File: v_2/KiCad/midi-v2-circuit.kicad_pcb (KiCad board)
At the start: 2 copper layers, 40 parts, among them CON1 IDC-14, CON2 AVR-ISP-10, CON3 IDC-14, J1 Screw_Terminal_01x12, J2 Conn_01x04, J3 DIN-8, J4 Conn_01x17, J6 USB_B, J7 to_midi_adapter_USB, J8 to_midi_adapter_MIDI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

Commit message: pcb first version complete - ready for hardware check and further optimalisation do 10x10cm
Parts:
- added REF**: MountingHole_4mm, Mounting_Holes:MountingHole_4mm, F.Cu at (255.9, 82.7)
- added REF**: MountingHole_2.5mm, Mounting_Holes:MountingHole_2.5mm, F.Cu at (269.4, 115.0)
- added REF**: MountingHole_4mm, Mounting_Holes:MountingHole_4mm, F.Cu at (255.9, 175.4)
- added REF**: MountingHole_4mm, Mounting_Holes:MountingHole_4mm, F.Cu at (347.3, 82.7)
- added REF**: MountingHole_4mm, Mounting_Holes:MountingHole_4mm, F.Cu at (347.3, 175.4)
- added REF**: MountingHole_2.5mm, Mounting_Holes:MountingHole_2.5mm, F.Cu at (269.4, 157.2)
- added REF**: MountingHole_2.5mm, Mounting_Holes:MountingHole_2.5mm, F.Cu at (284.7, 157.2)
- added REF**: MountingHole_2.5mm, Mounting_Holes:MountingHole_2.5mm, F.Cu at (284.7, 115.0)
- C1, C2, C5, C6, R1, R2, R3, R5, R8, R9: moved to B.Cu
- moved C10 231.3 mm to (332.7, 38.9)
- moved C11 231.3 mm to (332.7, 33.1)
- moved CON1 231.3 mm to (343.3, 54.8)
- moved J1 231.3 mm to (313.8, 68.5)
- moved C8 231.3 mm to (337.1, 33.1)
- moved C9 231.3 mm to (337.1, 38.9)
- moved REF** 231.3 mm to (306.1, 71.6)
- moved REF** 231.3 mm to (346.7, 30.9)
- moved REF** 231.3 mm to (306.1, 30.9)
- moved REF** 231.3 mm to (346.7, 71.6)
- moved RV1 231.3 mm to (326.4, 51.2)
- moved J7 91.5 mm to (273.4, 170.6), turned to 270 degrees
- moved CON3 67.4 mm to (343.6, 164.7), turned to 180 degrees
- moved R1 47.6 mm to (340.2, 115.4), turned to 180 degrees
- moved D1 35.6 mm to (267.8, 87.6)
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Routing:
- net GND: track 410.2 -> 603.6 mm, vias 0 -> 1
- net Net-(J6-Pad3): track 13.1 -> 114.2 mm
- net Net-(J6-Pad2): track 11.2 -> 111.8 mm
- net midi-raw-signal-power: track 29.6 -> 75.9 mm
- net SCL: track 21.2 -> 53.3 mm, vias 0 -> 1
- net joystick-pot-1: track 95.8 -> 68.0 mm
- net +5V: track 424.2 -> 450.2 mm, vias 0 -> 3
- net joystick-pot-2: track 86.2 -> 62.3 mm
- net button-4: track 79.9 -> 103.8 mm
- net MISO: track 122.9 -> 146.6 mm
- net Net-(D1-Pad2): track 10.8 -> 33.6 mm
- net RST: track 83.7 -> 63.4 mm
- net button-3: track 74.2 -> 94.3 mm
- net VCC: track 47.2 -> 27.7 mm
- net knob-pot-4: track 79.0 -> 61.0 mm
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
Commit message: adc first success
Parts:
- removed the REF** at (255.9, 82.7)
- removed the REF** at (306.1, 71.6)
- removed the REF** at (255.9, 175.4)
- removed the REF** at (347.3, 82.7)
- removed the REF** at (347.3, 175.4)
- removed the REF** at (346.7, 30.9)
- removed the REF** at (306.1, 30.9)
- removed the REF** at (346.7, 71.6)
- added R10: 330, Resistors_SMD:R_0805_HandSoldering, B.Cu at (97.0, 95.2)
- added R11: 330, Resistors_SMD:R_0805_HandSoldering, B.Cu at (97.0, 93.0)
- added R12: 330, Resistors_SMD:R_0805_HandSoldering, B.Cu at (97.0, 90.7)
- added R13: 330, Resistors_SMD:R_0805_HandSoldering, B.Cu at (97.0, 88.4)
- added R6: 330, Resistors_SMD:R_0805_HandSoldering, B.Cu at (97.0, 99.8)
- added R7: 330, Resistors_SMD:R_0805_HandSoldering, B.Cu at (97.0, 97.5)
- added REF**: MountingHole_4mm, Mounting_Holes:MountingHole_4mm, F.Cu at (193.2, 107.6)
- added REF**: MountingHole_2.2mm_M2, Mounting_Holes:MountingHole_2.2mm_M2, F.Cu at (106.6, 107.2)
- added REF**: MountingHole_2.2mm_M2, Mounting_Holes:MountingHole_2.2mm_M2, F.Cu at (87.5, 81.8)
- added REF**: MountingHole_2.2mm_M2, Mounting_Holes:MountingHole_2.2mm_M2, F.Cu at (106.6, 81.8)
- added REF**: MountingHole_2.2mm_M2, Mounting_Holes:MountingHole_2.2mm_M2, F.Cu at (87.5, 107.2)
- added REF**: MountingHole_4mm, Mounting_Holes:MountingHole_4mm, F.Cu at (132.5, 107.6)
- added REF**: MountingHole_4mm, Mounting_Holes:MountingHole_4mm, F.Cu at (81.7, 58.0)
- added REF**: MountingHole_4mm, Mounting_Holes:MountingHole_4mm, F.Cu at (193.2, 58.0)
- C3, C4, C7, R4: moved to B.Cu
- L1: footprint Inductors_SMD:L_1812_HandSoldering -> Inductors_SMD:L_0805_HandSoldering; moved to B.Cu
- moved CON1 261.2 mm to (84.1, 87.4), turned to 180 degrees
- moved C8 251.4 mm to (97.0, 107.8), turned to 90 degrees
- moved C9 244.0 mm to (103.0, 107.8), turned to 90 degrees
- moved C11 234.7 mm to (108.6, 102.5), turned to 0 degrees
- moved RV1 233.4 mm to (97.0, 94.5), turned to 180 degrees
- moved C10 232.2 mm to (108.7, 99.8), turned to 0 degrees
- moved R2 225.5 mm to (90.1, 66.7), turned to 180 degrees
- moved J2 222.0 mm to (83.8, 66.8), turned to 0 degrees
- moved R3 220.7 mm to (90.1, 70.9), turned to 180 degrees
- moved J1 200.8 mm to (113.4, 81.0), turned to 270 degrees
- moved R1 175.8 mm to (172.0, 64.4), turned to 270 degrees
- moved C4 173.7 mm to (157.7, 78.5), turned to 270 degrees
- moved SW2 172.9 mm to (176.3, 58.4), turned to 0 degrees
- moved C6 172.6 mm to (177.0, 78.6), turned to 90 degrees
- moved Y1 172.6 mm to (150.5, 73.5)
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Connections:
- J1 pad 10: button-2 -> button-4
- J1 pad 11: button-3 -> button-1
- J1 pad 12: button-4 -> button-2
- J1 pad 3: slide-pot-1 -> Net-(J1-Pad3)
- J1 pad 4: slide-pot-2 -> Net-(J1-Pad4)
- J1 pad 5: knob-pot-1 -> Net-(J1-Pad5)
- J1 pad 6: knob-pot-2 -> Net-(J1-Pad6)
- J1 pad 7: knob-pot-3 -> Net-(J1-Pad7)
- J1 pad 8: knob-pot-4 -> Net-(J1-Pad8)
- J1 pad 9: button-1 -> button-3
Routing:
- net GND: track 603.6 -> 123.3 mm, vias 1 -> 3
- net Net-(J6-Pad2): track 111.8 -> 24.5 mm
- net Net-(J6-Pad3): track 114.2 -> 30.0 mm
- net SDA: track 35.5 -> 117.1 mm
- net MOSI: track 169.6 -> 88.2 mm, vias 0 -> 1
- net MISO: track 146.6 -> 73.6 mm, vias 0 -> 1
- net +5V: track 450.2 -> 388.7 mm
- net SCL: track 53.3 -> 112.0 mm
- net button-2: track 112.4 -> 57.2 mm
- net SCK: track 140.3 -> 85.9 mm, vias 0 -> 1
- net button-1: track 99.4 -> 53.3 mm
- net slide-pot-1: track 76.4 -> 34.0 mm
- net slide-pot-2: track 74.5 -> 34.6 mm
- net midi-raw-signal-power: track 75.9 -> 37.3 mm
- net knob-pot-1: track 69.9 -> 34.0 mm
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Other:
- board outline added: 120.4 x 58.4 mm
- net class Default: via_dia 0.6 -> 1.2
- board text added: "MIDI v2"
- board text added: "by MM"

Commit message: improvements before first pcb order
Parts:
- removed the REF** at (138.3, 81.0)
- removed the REF** at (180.8, 98.5)
- added R14: 10k, Resistors_SMD:R_0805_HandSoldering, B.Cu at (143.3, 105.9)
- added R15: 10k, Resistors_SMD:R_0805_HandSoldering, B.Cu at (155.8, 70.9)
- added R16: 10k, Resistors_SMD:R_0805_HandSoldering, B.Cu at (163.0, 70.9)
- added R17: 10k, Resistors_SMD:R_0805_HandSoldering, B.Cu at (159.6, 70.9)
- added REF**: MountingHole_2.5mm, Mounting_Holes:MountingHole_2.5mm, F.Cu at (178.9, 83.2)
- added REF**: MountingHole_2.5mm, Mounting_Holes:MountingHole_2.5mm, F.Cu at (178.9, 95.3)
- moved REF** 45.0 mm to (135.9, 83.2)
- moved REF** 3.95 mm to (136.0, 95.3)
- moved J4 2.00 mm to (174.4, 105.9)
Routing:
- net GND: track 123.3 -> 164.4 mm
- net octave-1: track 59.6 -> 78.2 mm
- net SCK: track 85.9 -> 102.2 mm
- net MISO: track 73.6 -> 88.3 mm
- net MOSI: track 88.2 -> 100.8 mm
- net note-13: track 28.4 -> 31.7 mm
- net note-7: track 32.8 -> 36.1 mm
- net knob-pot-1: track 34.0 -> 36.9 mm
- net knob-pot-3: track 35.3 -> 37.8 mm
- net knob-pot-2: track 33.3 -> 35.6 mm
- net note-6: track 36.9 -> 38.9 mm
- net note-9: track 27.8 -> 29.8 mm
- net note-8: track 31.9 -> 33.9 mm
- net note-5: track 34.8 -> 36.8 mm
- net note-3: track 36.8 -> 38.8 mm
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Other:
- board text added: "MM 2018"
- board text removed: "by MM"

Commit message: tweaks before first order part 2
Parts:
- moved REF** 5.02 mm to (136.0, 78.2)
- moved REF** 4.95 mm to (179.0, 78.3)
- moved C6 3.18 mm to (173.9, 78.5)
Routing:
- net button-1: track 53.5 -> 62.0 mm
- net slide-pot-1: track 34.0 -> 38.5 mm
- net +5V: track 388.3 -> 384.5 mm
- net slide-pot-2: track 33.9 -> 37.5 mm
- net GND: track 164.4 -> 161.2 mm
- net midi-data-pin: track 51.6 -> 49.0 mm

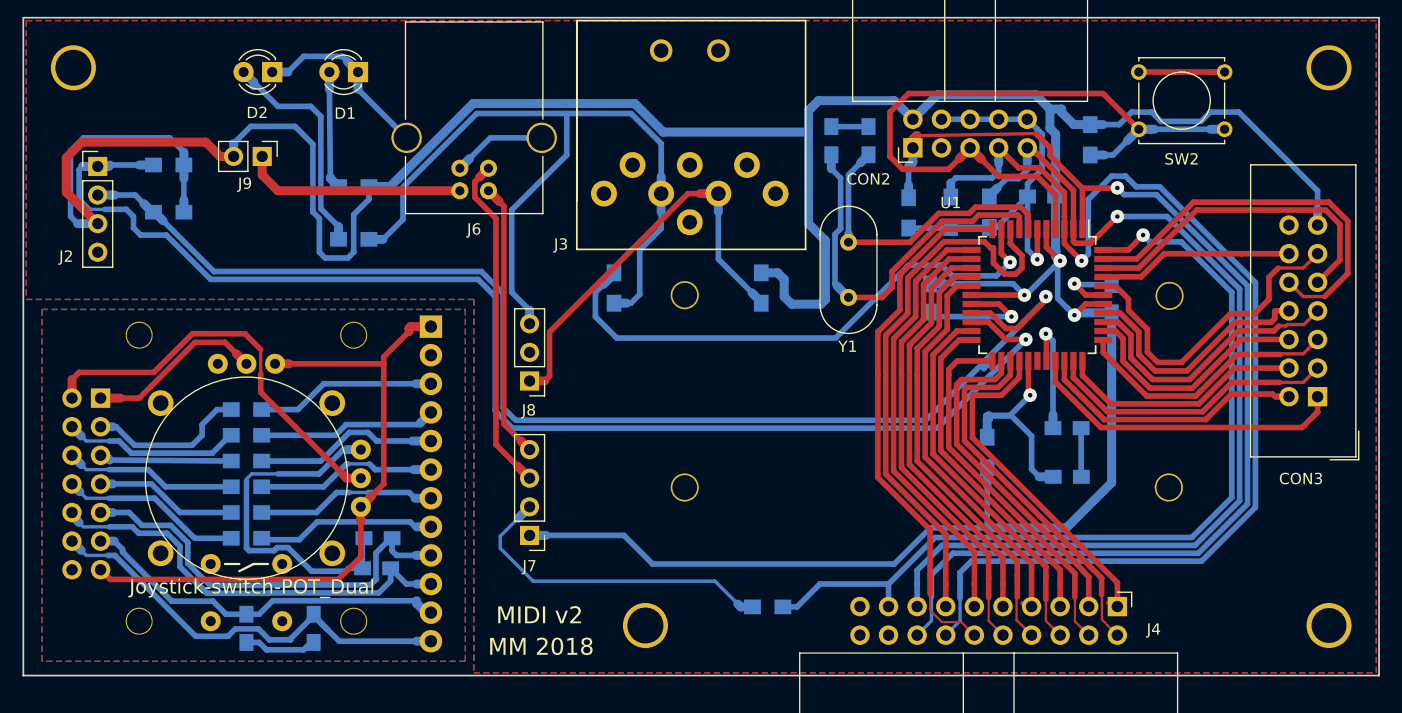
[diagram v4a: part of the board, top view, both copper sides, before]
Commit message: clearence changed to min 0.3 mm, resistor placement tweaks, ready for fabrication
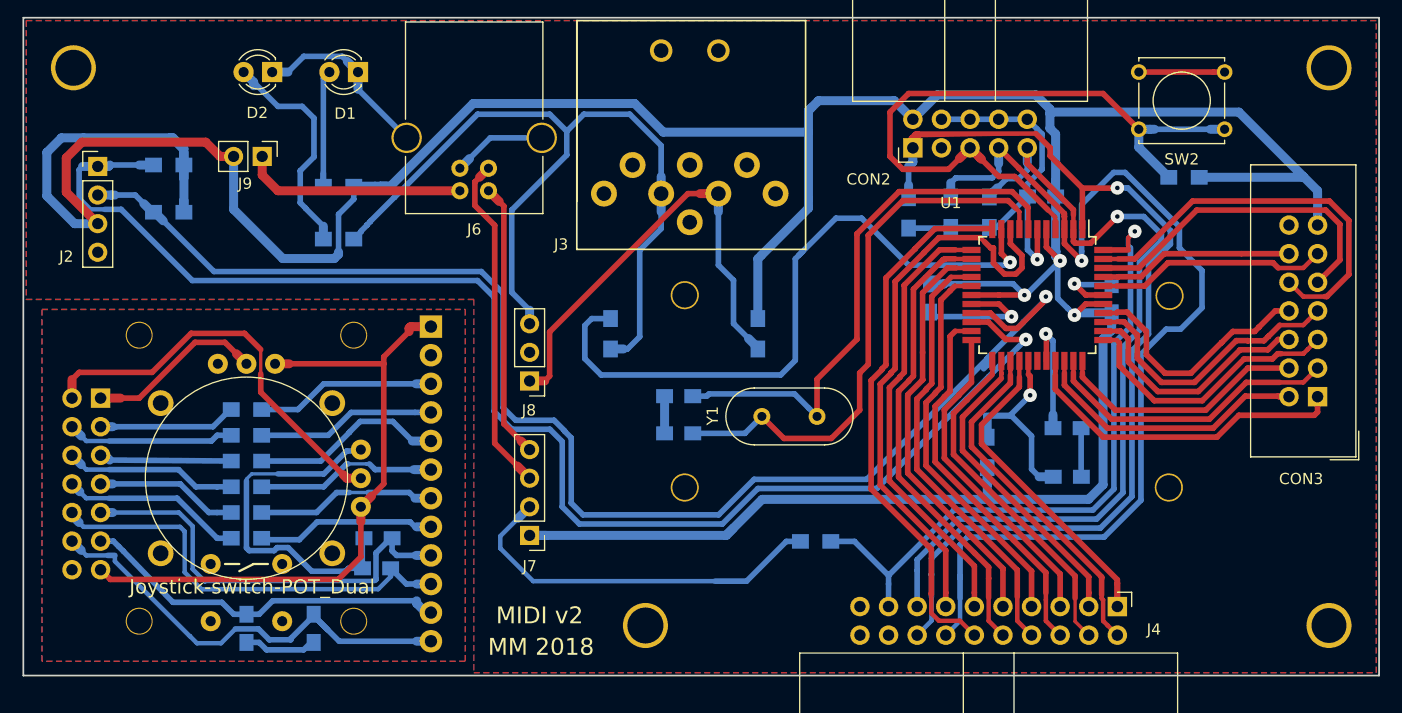
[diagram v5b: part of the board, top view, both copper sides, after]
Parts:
- moved C2 29.3 mm to (135.4, 90.5), turned to 180 degrees
- moved C1 28.3 mm to (135.4, 87.2), turned to 180 degrees
- moved Y1 15.7 mm to (147.7, 89.0), turned to 180 degrees
- moved R1 8.97 mm to (180.3, 67.8), turned to 180 degrees
- moved R14 7.21 mm to (147.6, 100.1)
- moved R4 4.08 mm to (129.4, 81.7)
- moved R5 4.08 mm to (142.4, 81.7)
- moved R8 1.35 mm to (105.2, 68.6)
- moved R9 1.35 mm to (105.2, 73.3)
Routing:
- net +5V: track 384.5 -> 412.1 mm
- net Net-(C1-Pad1): track 27.3 -> 48.9 mm
- net octave-1: track 78.2 -> 60.3 mm
- net Net-(C2-Pad1): track 33.9 -> 49.8 mm
- net MISO: track 88.3 -> 75.8 mm
- net midi-data-pin: track 49.0 -> 60.5 mm
- net SCL: track 112.7 -> 123.1 mm
- net SDA: track 117.1 -> 126.9 mm
- net SCK: track 102.2 -> 92.6 mm
- net button-1: track 62.0 -> 53.8 mm
- net midi-raw-signal-data: track 71.5 -> 76.5 mm
- net GND: track 161.2 -> 166.0 mm
- net midi-raw-signal-power: track 37.3 -> 41.2 mm
- net note-12: track 33.7 -> 31.2 mm
- net note-10: track 32.9 -> 30.8 mm
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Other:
- net class Default: clearance 0.2 -> 0.3
- net class pad-tracks added: clearance 0.2, trace_width 0.25, via_dia 1.2, via_drill 0.4
- rule pad_to_mask_clearance: 0.2 -> 0.3
- rule trace_clearance: 0.2 -> 0.3

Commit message: further tweaks, ready to order
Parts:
- RV1: value Joystick-switch-POT_Dual -> Joystick; moved to B.Cu
- moved C11 26.2 mm to (83.0, 107.8)
- moved REF** 8.89 mm to (123.6, 107.8)
- moved C10 4.75 mm to (107.5, 104.4)
- moved R9 4.09 mm to (105.2, 69.2)
- moved R8 3.20 mm to (105.2, 65.4)
- moved C9 3.08 mm to (99.9, 108.0), turned to 0 degrees
- moved REF** 3.00 mm to (179.0, 81.3)
- moved REF** 3.00 mm to (136.0, 81.2)
- moved REF** 3.00 mm to (136.0, 98.3)
- moved REF** 3.00 mm to (178.9, 98.3)
- moved C8 2.31 mm to (94.7, 108.0), turned to 180 degrees
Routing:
- net GND: track 166.0 -> 271.3 mm, vias 3 -> 4
- net button-1: track 53.8 -> 98.0 mm, vias 0 -> 1
- net button-3: track 68.1 -> 109.1 mm
- net SCL: track 123.1 -> 110.5 mm
- net button-2: track 58.0 -> 70.2 mm
- net MOSI: track 99.2 -> 88.1 mm
- net +5V: track 412.1 -> 402.3 mm
- net midi-data-pin: track 60.5 -> 51.3 mm
- net joystick-pot-2: track 45.7 -> 53.3 mm
- net SDA: track 126.9 -> 120.2 mm
- net Net-(D2-Pad2): track 21.6 -> 15.3 mm
- net midi-raw-signal-data: track 76.5 -> 70.6 mm
- net Net-(D1-Pad2): track 11.5 -> 7.91 mm
- net button-4: track 75.6 -> 79.1 mm
- net joystick-pot-1: track 61.4 -> 58.8 mm
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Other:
- net class Default: clearance 0.3 -> 0.2
- rule trace_clearance: 0.3 -> 0.2
- board text added: "+5V"
- board text added: "BUTTONS"
- board text added: "D+"
- board text added: "D-"
- board text added: "DATA"
- board text added: "GND"
- board text added: "JOYSTICK BOARD"
- board text added: "KEYBOARD"
- board text added: "MIDI +"
- board text added: "MIDI -"
- board text added: "MIDI - USB Adapter"
- board text added: "MIDI v2 rev.1"
- board text added: "POTENTIOMETERS"
- board text added: "PWR"
- board text added: "PWR SWITCH"
- board text added: "SCL"
- board text added: "SDA"
- board text removed: "MIDI v2"

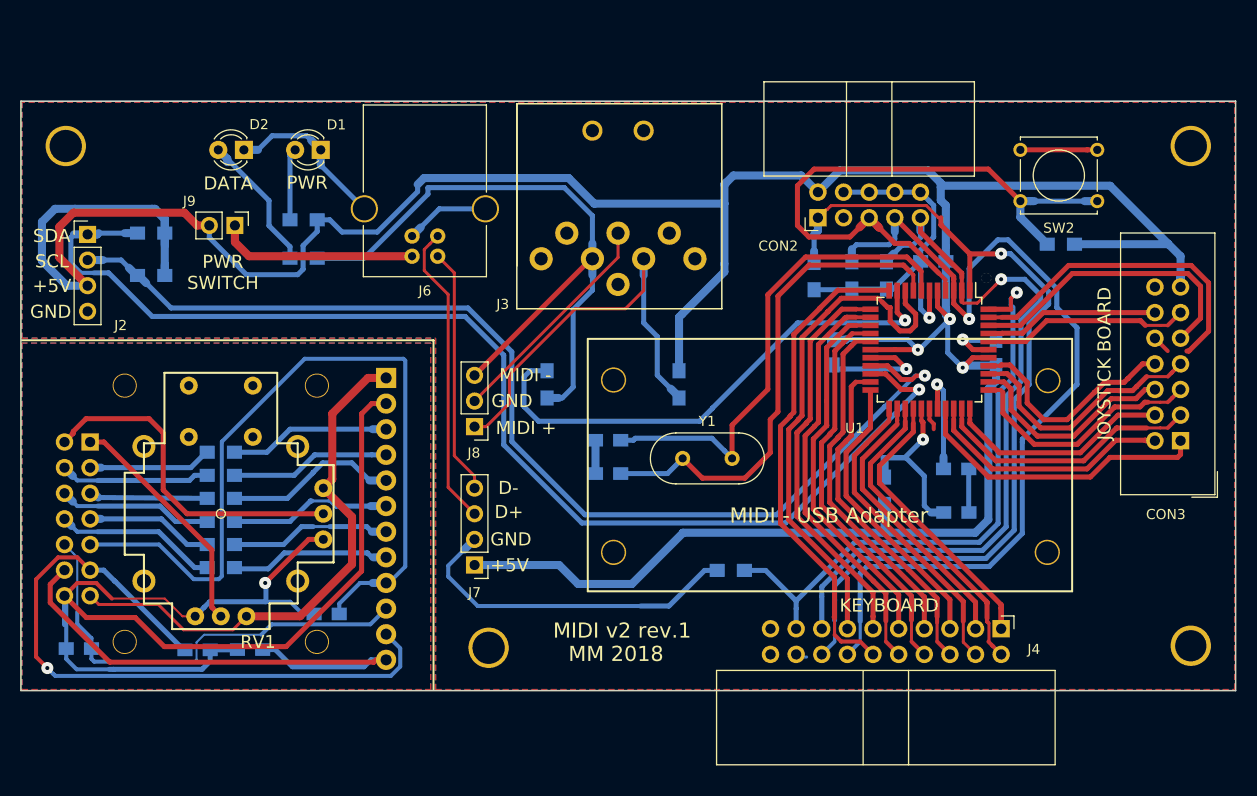
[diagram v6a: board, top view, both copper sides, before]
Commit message: resized to max 10x10cm - ordering at JLCPCB
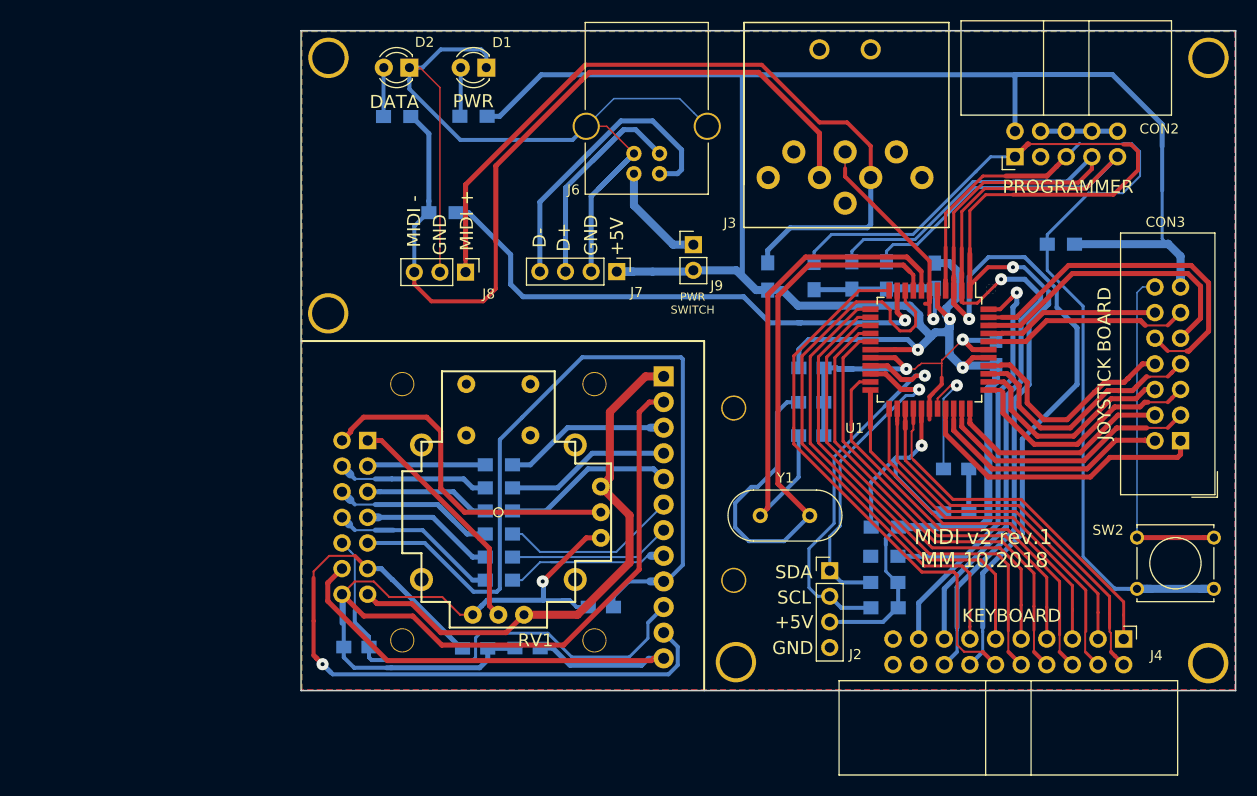
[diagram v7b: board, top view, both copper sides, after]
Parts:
- removed the REF** at (179.0, 81.3)
- removed the REF** at (136.0, 81.2)
- removed the REF** at (136.0, 98.3)
- removed the REF** at (178.9, 98.3)
- added REF**: MountingHole_4mm, Mounting_Holes:MountingHole_4mm, F.Cu at (107.7, 74.6)
- added REF**: MountingHole_2.5mm, Mounting_Holes:MountingHole_2.5mm, F.Cu at (147.9, 84.0)
- added REF**: MountingHole_2.5mm, Mounting_Holes:MountingHole_2.5mm, F.Cu at (147.9, 101.1)
- moved J2 80.8 mm to (157.4, 100.1)
- moved R2 80.5 mm to (162.8, 101.3)
- moved R3 79.8 mm to (162.8, 103.8)
- moved J9 45.5 mm to (143.9, 67.8), turned to 0 degrees
- moved SW2 40.1 mm to (187.8, 96.9)
- moved J7 32.3 mm to (136.3, 70.5), turned to 270 degrees
- moved R10 27.6 mm to (124.6, 96.5)
- moved R11 27.6 mm to (124.6, 94.2)
- moved R12 27.6 mm to (124.6, 91.9)
- moved R13 27.6 mm to (124.6, 89.6)
- moved R6 27.6 mm to (124.6, 101.1)
- moved R7 27.6 mm to (124.6, 98.8)
- moved REF** 27.5 mm to (134.1, 107.0)
- moved REF** 27.5 mm to (134.1, 81.6)
- moved C11 27.5 mm to (110.5, 107.7)
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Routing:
- net SDA: track 120.2 -> 32.1 mm
- net +5V: track 402.3 -> 318.7 mm
- net SCL: track 110.5 -> 39.4 mm
- net GND: track 271.3 -> 342.1 mm
- net RST: track 60.6 -> 101.8 mm
- net midi-raw-signal-power: track 42.4 -> 77.4 mm
- net MOSI: track 88.1 -> 120.1 mm
- net MISO: track 75.8 -> 104.4 mm
- net SCK: track 91.8 -> 114.3 mm
- net midi-raw-signal-data: track 70.6 -> 88.1 mm
- net Net-(C2-Pad1): track 49.8 -> 64.8 mm
- net octave-1: track 60.3 -> 49.4 mm
- net Net-(D2-Pad2): track 15.3 -> 4.86 mm
- net note-8: track 33.8 -> 43.0 mm
- net VCC: track 19.8 -> 10.7 mm
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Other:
- board size 120.4 x 58.4 mm -> 92.6 x 65.4 mm
- net class Default: clearance 0.2 -> 0.3
- rule trace_clearance: 0.2 -> 0.3
- rule trace_min: 0.1 -> 0.2
- board text added: "MM 10.2018"
- board text added: "PROGRAMMER"
- board text removed: "MIDI - USB Adapter"
- board text removed: "MM 2018"
